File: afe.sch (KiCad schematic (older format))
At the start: 57 parts, among them J3 Conn_01x05, Q6 AO3400, Q7 AO3400, Q8 AO3400, Q9 AO3400, U10 TS5A2053, U11 TS5A2053, U12 ADS7946SRTET, U5 REF2915, U6 TCA9535MRGER, U7 TLV9062S, U8 OPA2322S, U9 USBLC6-4SC6

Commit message: ADD:started to place footprints
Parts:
- C10, C11, C12, C13, C14, C16, C17, C18, C19, C20, C21, C22, C9: footprint Capacitor_SMD:C_0603_1608Metric -> Capacitor_SMD:C_0402_1005Metric
- R22, R23, R24, R25, R26, R27, R28, R29, R30, R31, R32, R37, R38, R39, R40, R41, R42, R43, R44: footprint Resistor_SMD:R_0603_1608Metric -> Resistor_SMD:R_0402_1005Metric
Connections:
- net PROBE1: now also U9.3 (IO2); no longer U9.4 (IO2)
- net PROBE2: now also U9.4 (IO2); no longer U9.3 (IO2)
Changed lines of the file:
@@
 F 0 "R26" V 3157 6250 50  0000 C CNN
 F 1 "100" V 3066 6250 50  0000 C CNN
-F 2 "Resistor_SMD:R_0603_1608Metric" V 2880 6250 50  0001 C CNN
+F 2 "Resistor_SMD:R_0402_1005Metric" V 2880 6250 50  0001 C CNN
 F 3 "~" H 2950 6250 50  0001 C CNN
 	1    2950 6250
@@
 F 0 "R23" H 1430 6354 50  0000 R CNN
 F 1 "47k" H 1430 6445 50  0000 R CNN
-F 2 "Resistor_SMD:R_0603_1608Metric" V 1430 6400 50  0001 C CNN
+F 2 "Resistor_SMD:R_0402_1005Metric" V 1430 6400 50  0001 C CNN
 F 3 "~" H 1500 6400 50  0001 C CNN
 	1    1500 6400
@@
 F 0 "R22" H 1430 5904 50  0000 R CNN
 F 1 "47k" H 1430 5995 50  0000 R CNN
-F 2 "Resistor_SMD:R_0603_1608Metric" V 1430 5950 50  0001 C CNN
+F 2 "Resistor_SMD:R_0402_1005Metric" V 1430 5950 50  0001 C CNN
 F 3 "~" H 1500 5950 50  0001 C CNN
 	1    1500 5950
@@
 F 0 "R25" H 2780 4454 50  0000 R CNN
 F 1 "680" H 2780 4545 50  0000 R CNN
-F 2 "Resistor_SMD:R_0603_1608Metric" V 2780 4500 50  0001 C CNN
+F 2 "Resistor_SMD:R_0402_1005Metric" V 2780 4500 50  0001 C CNN
 F 3 "~" H 2850 4500 50  0001 C CNN
 	1    2850 4500
@@
 F 0 "R27" H 3030 4204 50  0000 R CNN
 F 1 "390k" H 3030 4295 50  0000 R CNN
-F 2 "Resistor_SMD:R_0603_1608Metric" V 3030 4250 50  0001 C CNN
+F 2 "Resistor_SMD:R_0402_1005Metric" V 3030 4250 50  0001 C CNN
 F 3 "~" H 3100 4250 50  0001 C CNN
 	1    3100 4250
@@
 F 0 "R28" H 3430 4454 50  0000 R CNN
 F 1 "680" H 3430 4545 50  0000 R CNN
-F 2 "Resistor_SMD:R_0603_1608Metric" V 3430 4500 50  0001 C CNN
+F 2 "Resistor_SMD:R_0402_1005Metric" V 3430 4500 50  0001 C CNN
 F 3 "~" H 3500 4500 50  0001 C CNN
 	1    3500 4500
@@
 F 0 "R29" H 3680 4204 50  0000 R CNN
 F 1 "390k" H 3680 4295 50  0000 R CNN
-F 2 "Resistor_SMD:R_0603_1608Metric" V 3680 4250 50  0001 C CNN
+F 2 "Resistor_SMD:R_0402_1005Metric" V 3680 4250 50  0001 C CNN
 F 3 "~" H 3750 4250 50  0001 C CNN
 	1    3750 4250
@@
 F 0 "R32" H 4080 4454 50  0000 R CNN
 F 1 "680" H 4080 4545 50  0000 R CNN
-F 2 "Resistor_SMD:R_0603_1608Metric" V 4080 4500 50  0001 C CNN
+F 2 "Resistor_SMD:R_0402_1005Metric" V 4080 4500 50  0001 C CNN
 F 3 "~" H 4150 4500 50  0001 C CNN
 	1    4150 4500
@@
 F 0 "R39" H 4330 4204 50  0000 R CNN
 F 1 "390k" H 4330 4295 50  0000 R CNN
-F 2 "Resistor_SMD:R_0603_1608Metric" V 4330 4250 50  0001 C CNN
+F 2 "Resistor_SMD:R_0402_1005Metric" V 4330 4250 50  0001 C CNN
 F 3 "~" H 4400 4250 50  0001 C CNN
 	1    4400 4250
@@
 F 0 "R41" V 6350 800 50  0000 C CNN
 F 1 "2M2" V 6350 1000 50  0000 C CNN
-F 2 "Resistor_SMD:R_0603_1608Metric" V 6180 900 50  0001 C CNN
+F 2 "Resistor_SMD:R_0402_1005Metric" V 6180 900 50  0001 C CNN
 F 3 "~" H 6250 900 50  0001 C CNN
 	1    6250 900
@@
 F 0 "C21" H 6742 1146 50  0000 L CNN
 F 1 "33p" H 6742 1055 50  0000 L CNN
-F 2 "Capacitor_SMD:C_0603_1608Metric" H 6650 1100 50  0001 C CNN
+F 2 "Capacitor_SMD:C_0402_1005Metric" H 6650 1100 50  0001 C CNN
 F 3 "~" H 6650 1100 50  0001 C CNN
 	1    6650 1100
@@
 F 0 "R43" V 7200 1100 50  0000 C CNN
 F 1 "10M" V 7000 1100 50  0000 C CNN
-F 2 "Resistor_SMD:R_0603_1608Metric" V 7030 1100 50  0001 C CNN
+F 2 "Resistor_SMD:R_0402_1005Metric" V 7030 1100 50  0001 C CNN
 F 3 "~" H 7100 1100 50  0001 C CNN
 	1    7100 1100
@@
 F 0 "C14" H 1842 5596 50  0000 L CNN
 F 1 "100n" H 1842 5505 50  0000 L CNN
-F 2 "Capacitor_SMD:C_0603_1608Metric" H 1750 5550 50  0001 C CNN
+F 2 "Capacitor_SMD:C_0402_1005Metric" H 1750 5550 50  0001 C CNN
 F 3 "~" H 1750 5550 50  0001 C CNN
 	1    1750 5550
@@
 F 0 "C19" V 6150 1150 50  0000 C CNN
 F 1 "1n" V 6150 950 50  0000 C CNN
-F 2 "Capacitor_SMD:C_0603_1608Metric" H 6250 1050 50  0001 C CNN
+F 2 "Capacitor_SMD:C_0402_1005Metric" H 6250 1050 50  0001 C CNN
 F 3 "~" H 6250 1050 50  0001 C CNN
 	1    6250 1050
@@
 F 0 "R42" V 6350 2100 50  0000 C CNN
 F 1 "2M2" V 6350 2300 50  0000 C CNN
-F 2 "Resistor_SMD:R_0603_1608Metric" V 6180 2200 50  0001 C CNN
+F 2 "Resistor_SMD:R_0402_1005Metric" V 6180 2200 50  0001 C CNN
 F 3 "~" H 6250 2200 50  0001 C CNN
 	1    6250 2200
@@
 F 0 "C20" V 6150 2450 50  0000 C CNN
 F 1 "1n" V 6150 2250 50  0000 C CNN
-F 2 "Capacitor_SMD:C_0603_1608Metric" H 6250 2350 50  0001 C CNN
+F 2 "Capacitor_SMD:C_0402_1005Metric" H 6250 2350 50  0001 C CNN
 F 3 "~" H 6250 2350 50  0001 C CNN
 	1    6250 2350
@@
 F 0 "R37" V 4300 1300 50  0000 C CNN
 F 1 "390k" V 4100 1300 50  0000 C CNN
-F 2 "Resistor_SMD:R_0603_1608Metric" V 4130 1300 50  0001 C CNN
+F 2 "Resistor_SMD:R_0402_1005Metric" V 4130 1300 50  0001 C CNN
 F 3 "~" H 4200 1300 50  0001 C CNN
 	1    4200 1300
@@
 F 0 "C17" H 4542 1346 50  0000 L CNN
 F 1 "6n8" H 4542 1255 50  0000 L CNN
-F 2 "Capacitor_SMD:C_0603_1608Metric" H 4450 1300 50  0001 C CNN
+F 2 "Capacitor_SMD:C_0402_1005Metric" H 4450 1300 50  0001 C CNN
 F 3 "~" H 4450 1300 50  0001 C CNN
 	1    4450 1300
@@
 F 0 "R30" V 3950 1150 50  0000 C CNN
 F 1 "390k" V 3750 1150 50  0000 C CNN
-F 2 "Resistor_SMD:R_0603_1608Metric" V 3780 1150 50  0001 C CNN
+F 2 "Resistor_SMD:R_0402_1005Metric" V 3780 1150 50  0001 C CNN
 F 3 "~" H 3850 1150 50  0001 C CNN
 	1    3850 1150
@@
 F 0 "R38" V 4300 2600 50  0000 C CNN
 F 1 "390k" V 4100 2600 50  0000 C CNN
-F 2 "Resistor_SMD:R_0603_1608Metric" V 4130 2600 50  0001 C CNN
+F 2 "Resistor_SMD:R_0402_1005Metric" V 4130 2600 50  0001 C CNN
 F 3 "~" H 4200 2600 50  0001 C CNN
 	1    4200 2600
@@
 F 0 "C18" H 4542 2646 50  0000 L CNN
 F 1 "6n8" H 4542 2555 50  0000 L CNN
-F 2 "Capacitor_SMD:C_0603_1608Metric" H 4450 2600 50  0001 C CNN
+F 2 "Capacitor_SMD:C_0402_1005Metric" H 4450 2600 50  0001 C CNN
 F 3 "~" H 4450 2600 50  0001 C CNN
 	1    4450 2600
@@
 F 0 "R31" V 3950 2450 50  0000 C CNN
 F 1 "390k" V 3750 2450 50  0000 C CNN
-F 2 "Resistor_SMD:R_0603_1608Metric" V 3780 2450 50  0001 C CNN
+F 2 "Resistor_SMD:R_0402_1005Metric" V 3780 2450 50  0001 C CNN
 F 3 "~" H 3850 2450 50  0001 C CNN
 	1    3850 2450
@@
 F 0 "C22" H 6742 2446 50  0000 L CNN
 F 1 "33p" H 6742 2355 50  0000 L CNN
-F 2 "Capacitor_SMD:C_0603_1608Metric" H 6650 2400 50  0001 C CNN
+F 2 "Capacitor_SMD:C_0402_1005Metric" H 6650 2400 50  0001 C CNN
 F 3 "~" H 6650 2400 50  0001 C CNN
 	1    6650 2400
@@
 F 0 "R44" V 7200 2400 50  0000 C CNN
 F 1 "10M" V 7000 2400 50  0000 C CNN
-F 2 "Resistor_SMD:R_0603_1608Metric" V 7030 2400 50  0001 C CNN
+F 2 "Resistor_SMD:R_0402_1005Metric" V 7030 2400 50  0001 C CNN
 F 3 "~" H 7100 2400 50  0001 C CNN
 	1    7100 2400
@@
 F 0 "C16" H 2142 1396 50  0000 L CNN
 F 1 "100n" H 2142 1305 50  0000 L CNN
-F 2 "Capacitor_SMD:C_0603_1608Metric" H 2050 1350 50  0001 C CNN
+F 2 "Capacitor_SMD:C_0402_1005Metric" H 2050 1350 50  0001 C CNN
 F 3 "~" H 2050 1350 50  0001 C CNN
 	1    2050 1350
@@
 F 0 "C13" H 1792 1396 50  0000 L CNN
 F 1 "100n" H 1792 1305 50  0000 L CNN
-F 2 "Capacitor_SMD:C_0603_1608Metric" H 1700 1350 50  0001 C CNN
+F 2 "Capacitor_SMD:C_0402_1005Metric" H 1700 1350 50  0001 C CNN
 F 3 "~" H 1700 1350 50  0001 C CNN
 	1    1700 1350
@@
 F 0 "C11" H 1442 1396 50  0000 L CNN
 F 1 "100n" H 1442 1305 50  0000 L CNN
-F 2 "Capacitor_SMD:C_0603_1608Metric" H 1350 1350 50  0001 C CNN
+F 2 "Capacitor_SMD:C_0402_1005Metric" H 1350 1350 50  0001 C CNN
 F 3 "~" H 1350 1350 50  0001 C CNN
 	1    1350 1350
@@
 F 0 "C10" H 1092 1396 50  0000 L CNN
 F 1 "100n" H 1092 1305 50  0000 L CNN
-F 2 "Capacitor_SMD:C_0603_1608Metric" H 1000 1350 50  0001 C CNN
+F 2 "Capacitor_SMD:C_0402_1005Metric" H 1000 1350 50  0001 C CNN
 F 3 "~" H 1000 1350 50  0001 C CNN
 	1    1000 1350
@@
 F 0 "C9" H 742 1396 50  0000 L CNN
 F 1 "100n" H 742 1305 50  0000 L CNN
-F 2 "Capacitor_SMD:C_0603_1608Metric" H 650 1350 50  0001 C CNN
+F 2 "Capacitor_SMD:C_0402_1005Metric" H 650 1350 50  0001 C CNN
 F 3 "~" H 650 1350 50  0001 C CNN
 	1    650  1350
@@
 F 0 "C12" H 1542 4996 50  0000 L CNN
 F 1 "100n" H 1542 4905 50  0000 L CNN
-F 2 "Capacitor_SMD:C_0603_1608Metric" H 1450 4950 50  0001 C CNN
+F 2 "Capacitor_SMD:C_0402_1005Metric" H 1450 4950 50  0001 C CNN
 F 3 "~" H 1450 4950 50  0001 C CNN
 	1    1450 4950
@@
 	1    0    0    -1
 $EndComp
+Text GLabel 5900 5000 2    50   Input ~ 0
+PROBE1
 Text GLabel 5900 4800 2    50   Input ~ 0
-PROBE1
-Text GLabel 5900 5000 2    50   Input ~ 0
 PROBE2
 Wire Wire Line
@@
 F 0 "R40" H 5930 3304 50  0000 R CNN
 F 1 "47k" H 5930 3395 50  0000 R CNN
-F 2 "Resistor_SMD:R_0603_1608Metric" V 5930 3350 50  0001 C CNN
+F 2 "Resistor_SMD:R_0402_1005Metric" V 5930 3350 50  0001 C CNN
 F 3 "~" H 6000 3350 50  0001 C CNN
 	1    6000 3350
@@
 F 0 "R24" H 2080 6854 50  0000 R CNN
 F 1 "47k" H 2080 6945 50  0000 R CNN
-F 2 "Resistor_SMD:R_0603_1608Metric" V 2080 6900 50  0001 C CNN
+F 2 "Resistor_SMD:R_0402_1005Metric" V 2080 6900 50  0001 C CNN
 F 3 "~" H 2150 6900 50  0001 C CNN
 	1    2150 6900

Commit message: ADD: started routing
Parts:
- added C35, C36: 470p, Capacitor_SMD:C_0402_1005Metric, symbol Device:C_Small
- added R52, R53: 10, Resistor_SMD:R_0603_1608Metric, symbol Device:R
- U7, U8: footprint Package_SON:VSON-10-1EP_3x3mm_P0.5mm_EP1.2x2mm -> badgelib:VSSOP-10
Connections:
- net GNDA: now also C35.2, C36.1
- net at U8.1, U8.2 (-): now also R52.2; no longer U12.5 (AIN0)
- net at U8.8 (-), U8.9: now also R53.2; no longer U12.8 (AIN1)
- new net: C35.1, R52.1, U12.5 (AIN0)
- new net: C36.2, R53.1, U12.8 (AIN1)
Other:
- moved on the sheet: C23, FB1, R40, U12

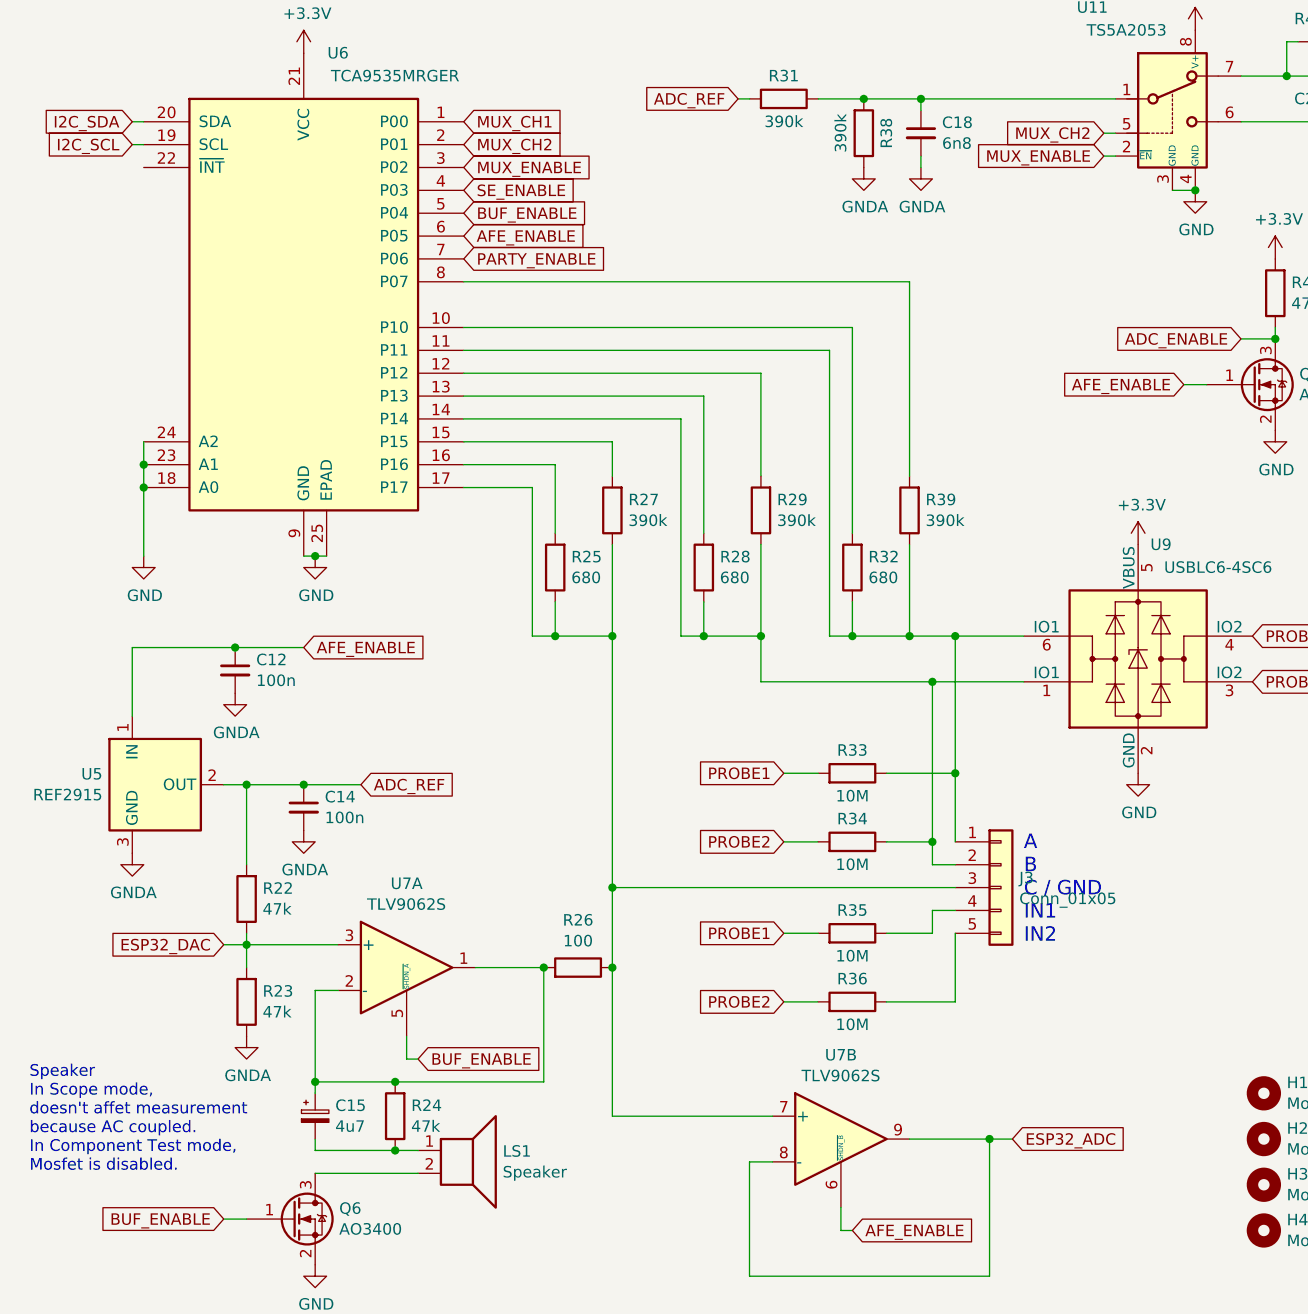
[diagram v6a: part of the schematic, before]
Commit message: fixed label and unconnected net
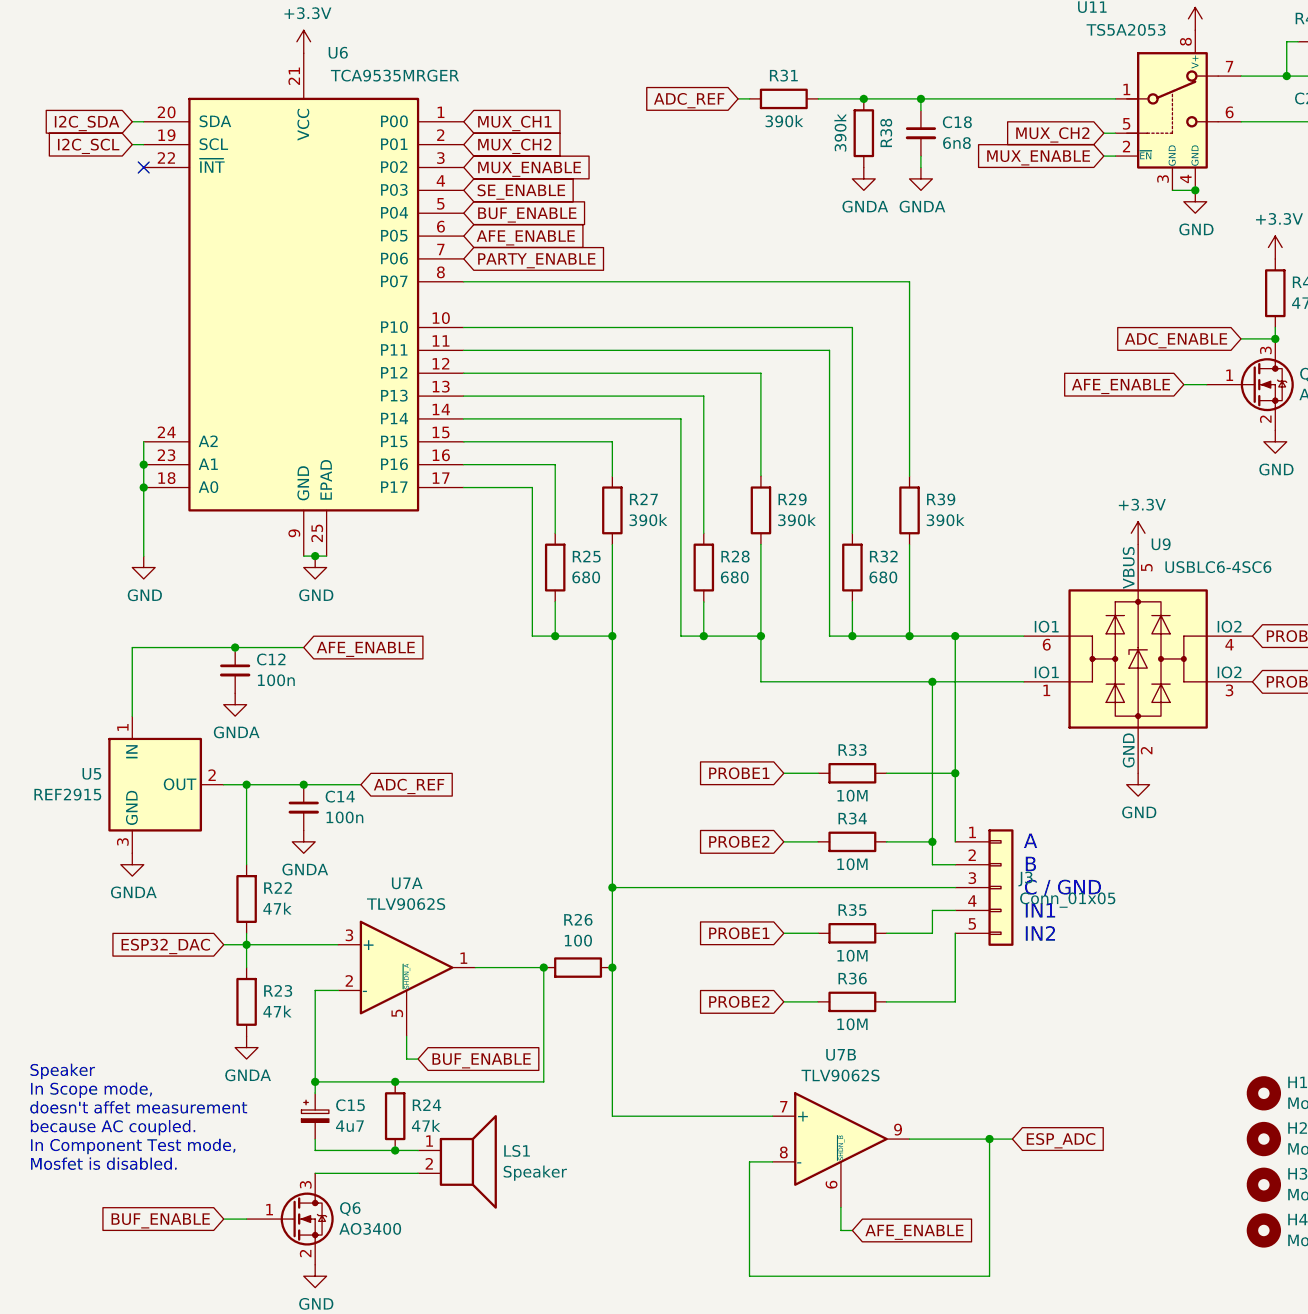
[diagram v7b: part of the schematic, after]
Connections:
- net ESP32_ADC renamed ESP_ADC
- no-connect marks 0 -> 1
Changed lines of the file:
@@
 $EndComp
 Text GLabel 4850 7000 2    50   Input ~ 0
-ESP32_ADC
+ESP_ADC
 $Comp
 L Device:R R23
@@
 	6000 3450 6000 3500
 Connection ~ 6000 3500
+NoConn ~ 1050 2750
 $EndSCHEMATC

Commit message: Finished layout
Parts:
- added C37: 470p, Capacitor_SMD:C_0402_1005Metric, symbol Device:C_Small
- added R50: 10, Resistor_SMD:R_0603_1608Metric, symbol Device:R
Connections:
- net ESP_ADC: now also C37.1, R50.1; no longer U7.8 (-), U7.9
- net GND: now also C37.2
- new net: R50.2, U7.8 (-), U7.9
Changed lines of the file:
@@
 	0    1    -1   0
 $EndComp
-Text GLabel 4850 7000 2    50   Input ~ 0
-ESP_ADC
 $Comp
 L Device:R R23
@@
 Connection ~ 6000 3500
 NoConn ~ 1050 2750
+$Comp
+L Device:R R50
+U 1 1 5C7E293A
+P 5000 7000
+F 0 "R50" V 5100 6900 50  0000 C CNN
+F 1 "10" V 5100 7100 50  0000 C CNN
+F 2 "Resistor_SMD:R_0603_1608Metric" V 4930 7000 50  0001 C CNN
+F 3 "~" H 5000 7000 50  0001 C CNN
+	1    5000 7000
+	0    1    -1   0
+$EndComp
+$Comp
+L Device:C_Small C37
+U 1 1 5C7E2F4C
+P 5200 7100
+F 0 "C37" H 5292 7146 50  0000 L CNN
+F 1 "470p" H 5292 7055 50  0000 L CNN
+F 2 "Capacitor_SMD:C_0402_1005Metric" H 5200 7100 50  0001 C CNN
+F 3 "~" H 5200 7100 50  0001 C CNN
+	1    5200 7100
+	1    0    0    -1
+$EndComp
+$Comp
+L power:GND #PWR0116
+U 1 1 5C7E341A
+P 5200 7200
+F 0 "#PWR0116" H 5200 6950 50  0001 C CNN
+F 1 "GND" H 5205 7027 50  0000 C CNN
+F 2 "" H 5200 7200 50  0001 C CNN
+F 3 "" H 5200 7200 50  0001 C CNN
+	1    5200 7200
+	1    0    0    -1
+$EndComp
+Text GLabel 5450 7000 2    50   Input ~ 0
+ESP_ADC
+Wire Wire Line
+	5450 7000 5200 7000
+Connection ~ 5200 7000
+Wire Wire Line
+	5200 7000 5150 7000
 $EndSCHEMATC
